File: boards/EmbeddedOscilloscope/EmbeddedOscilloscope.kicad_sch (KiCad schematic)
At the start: 0 parts

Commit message: Buck converter and battery backpack
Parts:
- added C1: 22uf, CC0805MKX5R5BB226:CC0805MKX5R5BB226, symbol CC0805MKX5R5BB226:CERAMIC-22UF-6.3V-20_-X5R_0805_
- added C2, C3, C4: 10uF, CC0805KKX5R5BB106:CC0805KKX5R5BB106, symbol CC0805KKX5R5BB106:CC0805KKX5R5BB106
- added D1: GREEN LED (DONE), 150080GS75000:150080GS75000, symbol 150080GS75000:WL-SMCW_0805
- added D2: RED LED (CHARGING), 150080SS75000:150080SS75000, symbol 150080SS75000:WL-SMCW_0805
- added J1: S2B-PH-SM4-TB, S2B-PH-SM4-TB:S2B-PH-SM4-TB, symbol S2B-PH-SM4-TB:S2B-PH-SM4-TB
- added JP1: SolderJumper, symbol Jumper:SolderJumper_2_Open
- added L1: 2.2uH, NRH2412T2R2MNGH:NRH2412T2R2MNGH, symbol NRH2412T2R2MNGH:NRH2412T2R2MNGH
- added R1: 100K, RC0805FR-07100KL:RC0805FR-07100KL, symbol RC0805FR-07100KL:RC0805FR-07100KL
- added R2: 10K, AF0805FR-0710KL:AF0805FR-0710KL, symbol AF0805FR-0710KL:AF0805FR-0710KL
- added R3: 2.5K, RC0805FR-072K49L:RC0805FR-072K49L, symbol RC0805FR-072K49L:RC0805FR-072K49L
- added R4, R5: 1K, RE0805FRE071KL:RE0805FRE071KL, symbol RE0805FRE071KL:RE0805FRE071KL
- added SW1: SLIDE SWITCH, JS202011SCQN:JS202011SCQN, symbol JS202011SCQN:JS202011SCQN
- added U1: LM3671MFX-3.3_NOPB, LM3671MFX-3.3_NOPB:LM3671MFX-3.3_NOPB, symbol LM3671MFX-3.3_NOPB:LM3671MFX-3.3_NOPB
- added U2: MCP73831T-2ACI_OT, MCP73831T-2ACI-OT:MCP73831T-2ACI-OT, symbol MCP73831T-2ACI-OT:MCP73831T-2ACI_OT
- added U3: ESP32-WROOM-32E, ESP32-WROOM-32E:ESP32-WROOM-32E, symbol RF_Module:ESP32-WROOM-32E
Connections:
- new net: R4.1, R5.1, U2.1 (STAT)
- new net: C3.1, J1.2, U2.3 (VBAT)
- new net: JP1.2 (B), R2.2, U2.5 (PROG)
- new net: L1.1, U1.5 (SW)
- new net: JP1.1 (A), R3.2
- new net: D1.2, R5.2
- new net: D2.1, R4.2
- new net: R1.2, U1.3 (EN)
- new net +3.3V: C1.1, L1.2, U1.4 (FB), U3.2 (VDD)
- new net +5V: C2.1, R1.1, SW1.4, U1.1 (VIN)
- new net GND: C1.2, C2.2, C3.2, C4.2, D1.1, J1.1, R2.1, R3.1, U1.2 (GND), U2.2 (VSS), U3.1 (GND), U3.15 (GND), U3.38 (GND), U3.39 (GND)
- new net POLE_A: C4.1, D2.2, SW1.1, U2.4 (VDD)
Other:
- note added: "Battery Backpack"
- note added: "Buck Converter"
- note added: "Controller"

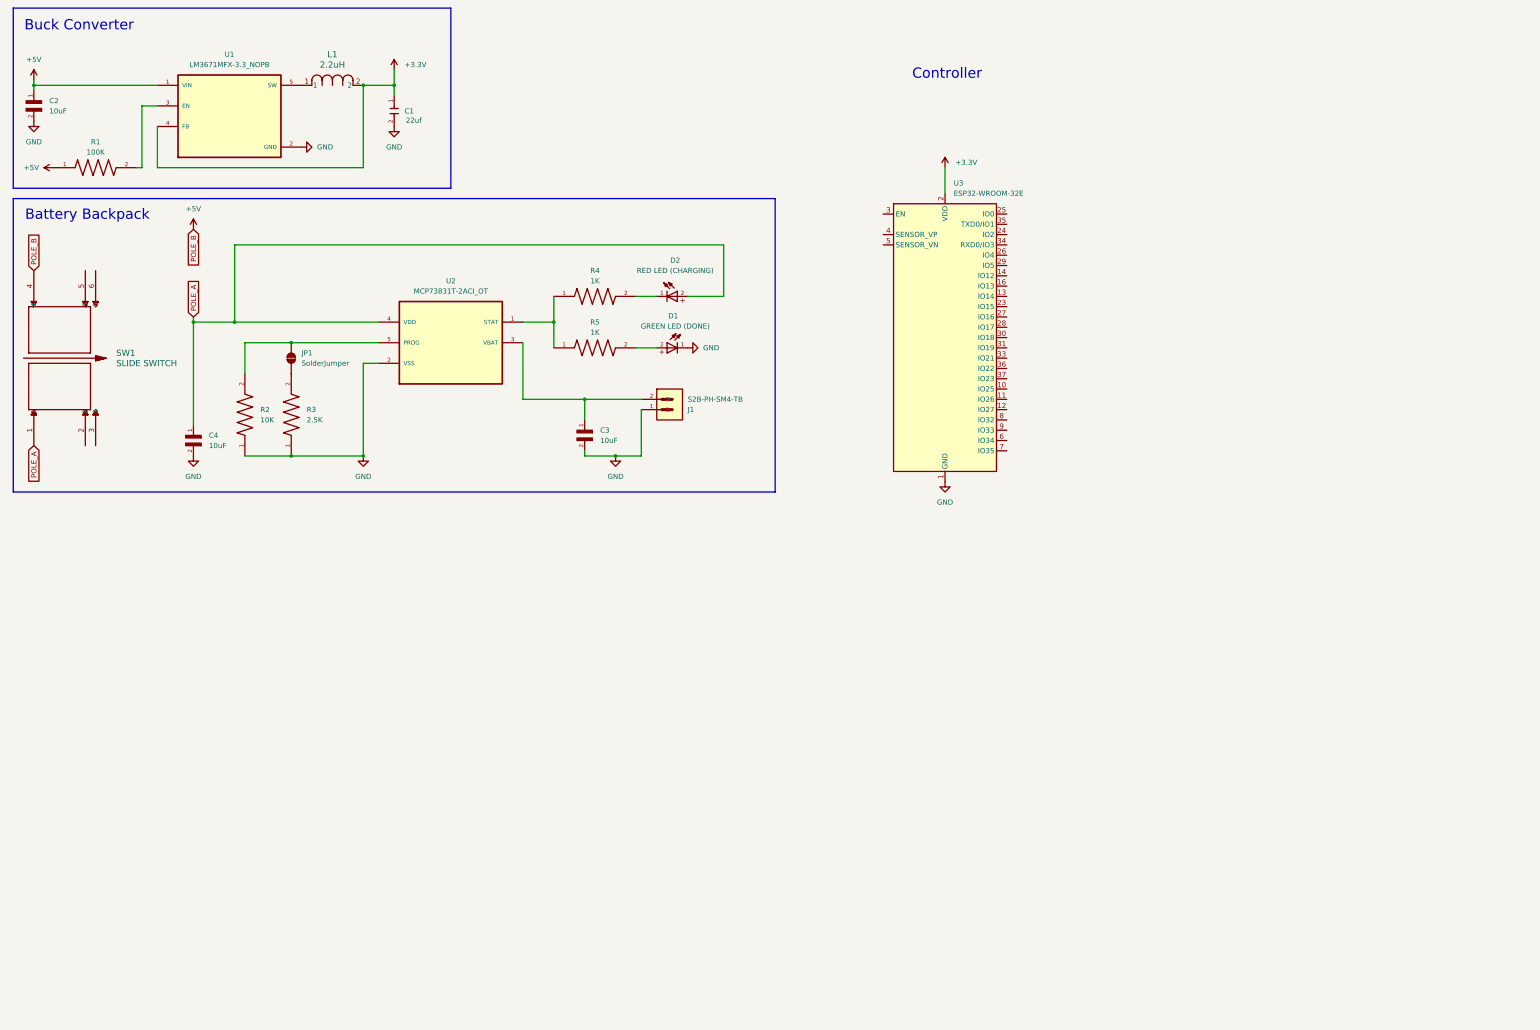
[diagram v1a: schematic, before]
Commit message: Embedded oscilloscope Fiverr delivery
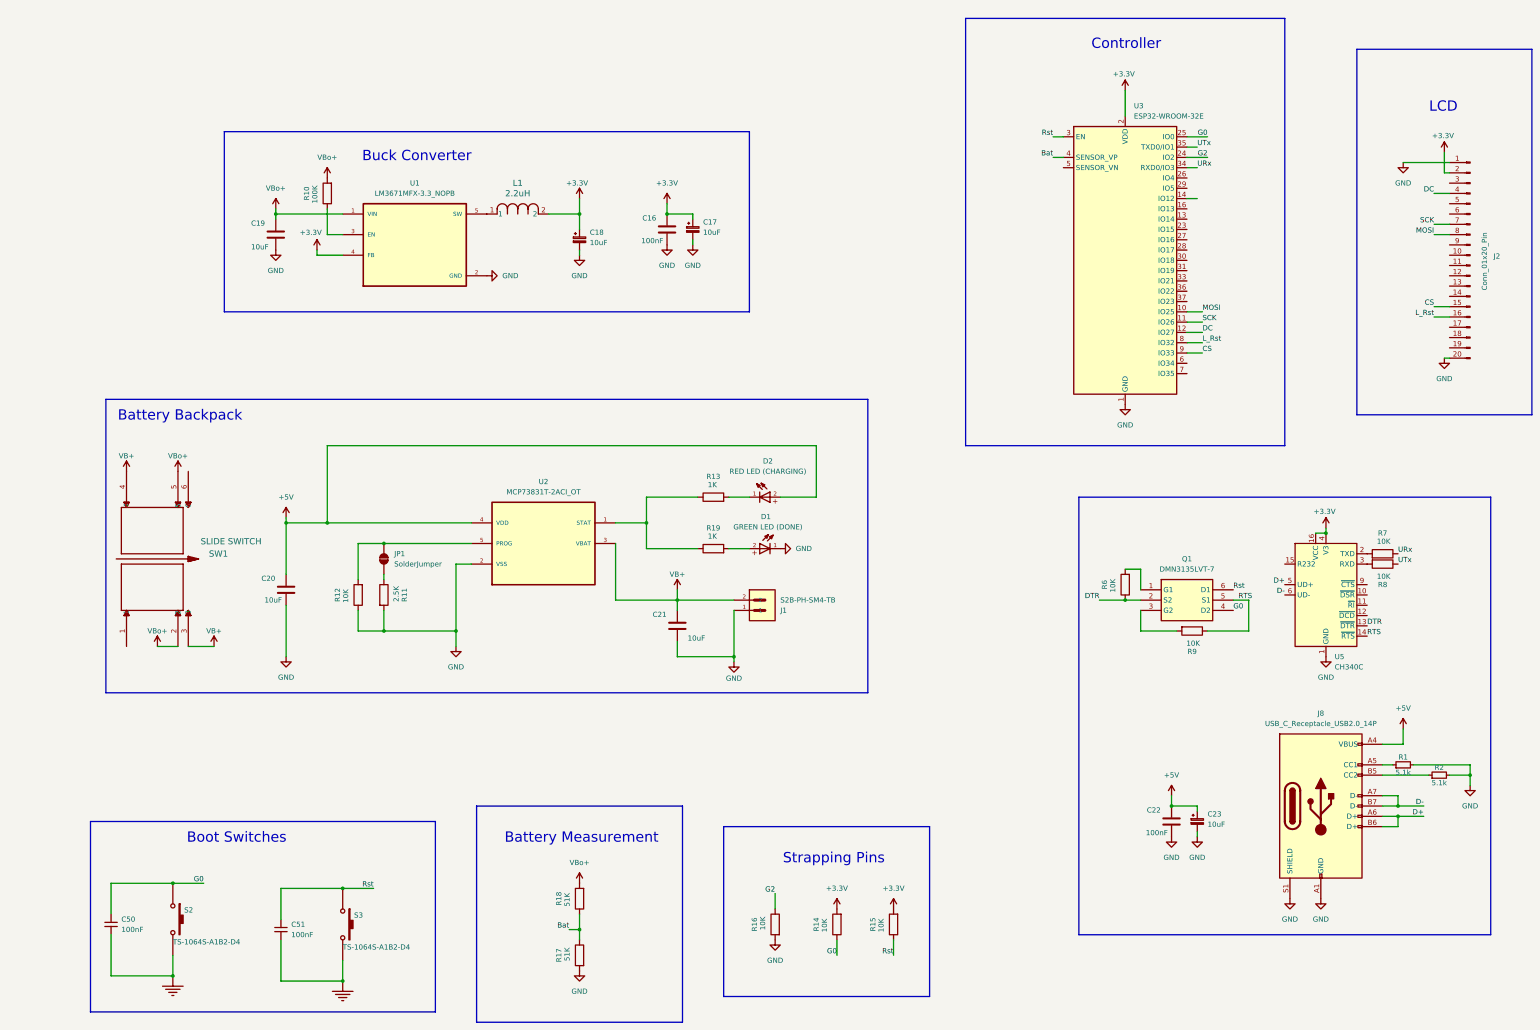
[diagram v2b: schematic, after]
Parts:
- removed C1: 22uf, CC0805MKX5R5BB226:CC0805MKX5R5BB226, symbol CC0805MKX5R5BB226:CERAMIC-22UF-6.3V-20_-X5R_0805_
- removed C2, C3, C4: 10uF, CC0805KKX5R5BB106:CC0805KKX5R5BB106, symbol CC0805KKX5R5BB106:CC0805KKX5R5BB106
- removed R1: 100K, RC0805FR-07100KL:RC0805FR-07100KL, symbol RC0805FR-07100KL:RC0805FR-07100KL
- removed R2: 10K, AF0805FR-0710KL:AF0805FR-0710KL, symbol AF0805FR-0710KL:AF0805FR-0710KL
- removed R3: 2.5K, RC0805FR-072K49L:RC0805FR-072K49L, symbol RC0805FR-072K49L:RC0805FR-072K49L
- removed R4, R5: 1K, RE0805FRE071KL:RE0805FRE071KL, symbol RE0805FRE071KL:RE0805FRE071KL
- added C16, C22: 100nF, Capacitor_SMD:C_0402_1005Metric, symbol Device:C
- added C17, C18, C23: 10uF, Capacitor_Tantalum_SMD:CP_EIA-3216-10_Kemet-I, symbol Device:C_Polarized_Small
- added C19, C20, C21: 10uF, Capacitor_SMD:C_0402_1005Metric, symbol Device:C
- added C50, C51: 100nF, Capacitor_SMD:C_0402_1005Metric, symbol Device:C_Small
- added J2: Conn_01x20_Pin, Connector_PinHeader_2.54mm:PinHeader_1x20_P2.54mm_Vertical, symbol Connector:Conn_01x20_Pin
- added J8: USB_C_Receptacle_USB2.0_14P, marbastlib-various.pretty:USB_C_Receptacle_HRO_TYPE-C-31-M-12, symbol Connector:USB_C_Receptacle_USB2.0_14P
- added Q1: DMN3135LVT-7, symbols:SOT95P280X100-6N, symbol DMN3135LVT-7:DMN3135LVT-7
- added R1, R2: 5.1k, Resistor_SMD:R_0402_1005Metric, symbol Device:R_Small
- added R10: 100K, Resistor_SMD:R_0402_1005Metric, symbol Device:R
- added R11: 2.5K, Resistor_SMD:R_0402_1005Metric, symbol Device:R
- added R12, R14, R15, R16, R6, R7, R8, R9: 10K, Resistor_SMD:R_0402_1005Metric, symbol Device:R
- added R13, R19: 1K, Resistor_SMD:R_0402_1005Metric, symbol Device:R
- added R17, R18: 51K, Resistor_SMD:R_0402_1005Metric, symbol Device:R
- added S2, S3: TS-1064S-A1B2-D4, KEY-SMD_L3.0-W2.5-LS4.0, symbol Sensor PCB-altium-import:root_3_SW-PB_Miscellaneous Devices.IntLib
- added U5: CH340C, Package_SO:SOIC-16_3.9x9.9mm_P1.27mm, symbol Interface_USB:CH340C
- D1: footprint 150080GS75000:150080GS75000 -> LED_SMD:LED_0603_1608Metric; LCSC Part Number (none) -> C12624
- D2: footprint 150080SS75000:150080SS75000 -> LED_SMD:LED_0603_1608Metric; LCSC Part Number (none) -> C2286
- J1: LCSC Part Number (none) -> C295747
- JP1: footprint (none) -> Jumper:SolderJumper-2_P1.3mm_Open_RoundedPad1.0x1.5mm
- L1: LCSC Part Number (none) -> C89149
- SW1: LCSC Part Number (none) -> C221666
- U1: LCSC Part Number (none) -> C477918
- U2: LCSC Part Number (none) -> C424093
- U3: LCSC Part Number (none) -> C701341
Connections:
- net +3.3V: now also C16.1, C17.1, C18.1, J2.2 (Pin_2), R14.2, R15.2, U5.16 (VCC), U5.4 (V3)
- net +5V: now also D2.2, U2.4 (VDD), C20.1, C22.1, C23.1, J8.A4 (VBUS), J8.A9 (VBUS), J8.B4 (VBUS), J8.B9 (VBUS); no longer SW1.4, U1.1 (VIN)
- net GND: now also C16.2, C17.2, C18.2, C19.2, C20.2, C21.2, C22.2, C23.2, C50.2, C51.2, J2.1 (Pin_1), J2.20 (Pin_20), J8.A1 (GND), J8.A12 (GND), J8.B1 (GND), J8.B12 (GND), J8.S1 (SHIELD), R1.2, R11.2, R12.1, R16.2, R17.2, R2.2, S2.2, S3.2, U5.1 (GND)
- net at U2.1 (STAT): now also R13.1, R19.1
- net VB+: now reaches J1.2, U2.3 (VBAT)
- net VB+: now also SW1.3, SW1.4, C21.1
- net at JP1.2 (B), U2.5 (PROG): now also R12.2
- net at JP1.1 (A): now also R11.1
- net at D1.2: now also R19.2
- net at D2.1: now also R13.2
- net at U1.3 (EN): now also R10.1
- net VBo+: now reaches SW1.2
- net VBo+: now also SW1.5, U1.1 (VIN), C19.1, R10.2, R18.2
- net MOSI: now reaches U3.10 (IO25)
- net MOSI: now also J2.8 (Pin_8)
- net SCK: now reaches U3.11 (IO26)
- net SCK: now also J2.7 (Pin_7)
- net DC: now reaches U3.12 (IO27)
- net DC: now also J2.4 (Pin_4)
- net G2: now reaches U3.24 (IO2)
- net G2: now also R16.1
- net G0: now reaches U3.25 (IO0)
- net G0: now also C50.1, Q1.4 (D2), R14.1, S2.1
- net Rst: now reaches U3.3 (EN)
- net Rst: now also C51.1, Q1.6 (D1), R15.1, S3.1
- net URx: now reaches U3.34 (RXD0/IO3)
- net URx: now also R7.1
- net UTx: now reaches U3.35 (TXD0/IO1)
- net UTx: now also R8.1
- net Bat: now reaches U3.4 (SENSOR_VP)
- net Bat: now also R17.1, R18.1
- net L_Rst: now reaches U3.8 (IO32)
- net L_Rst: now also J2.16 (Pin_16)
- net CS: now reaches U3.9 (IO33)
- net CS: now also J2.15 (Pin_15)
- removed net POLE_A: D2.2, SW1.1, U2.4 (VDD)
- new net: R7.2, U5.2 (TXD)
- new net: Q1.1 (G1), R6.2
- new net: R8.2, U5.3 (RXD)
- new net: J8.B5 (CC2), R2.1
- new net: Q1.3 (G2), R9.2
- new net: J8.A5 (CC1), R1.1
- new net D+: J8.A6 (D+), J8.B6 (D+), U5.5 (UD+)
- new net D-: J8.A7 (D-), J8.B7 (D-), U5.6 (UD-)
- new net DTR: Q1.2 (S2), R6.1, U5.13 (~{DTR})
- new net RTS: Q1.5 (S1), R9.1, U5.14 (~{RTS})
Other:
- note added: "Battery Measurement"
- note added: "Boot Switches"
- note added: "LCD"
- note added: "Strapping Pins"
- moved on the sheet: D1, D2, J1, JP1, L1, SW1, U1, U2, U3
